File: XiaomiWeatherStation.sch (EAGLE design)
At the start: 12 parts, among them J1 1X2-3.5MM, K1 RELAY-SPDT, Q1 BD437

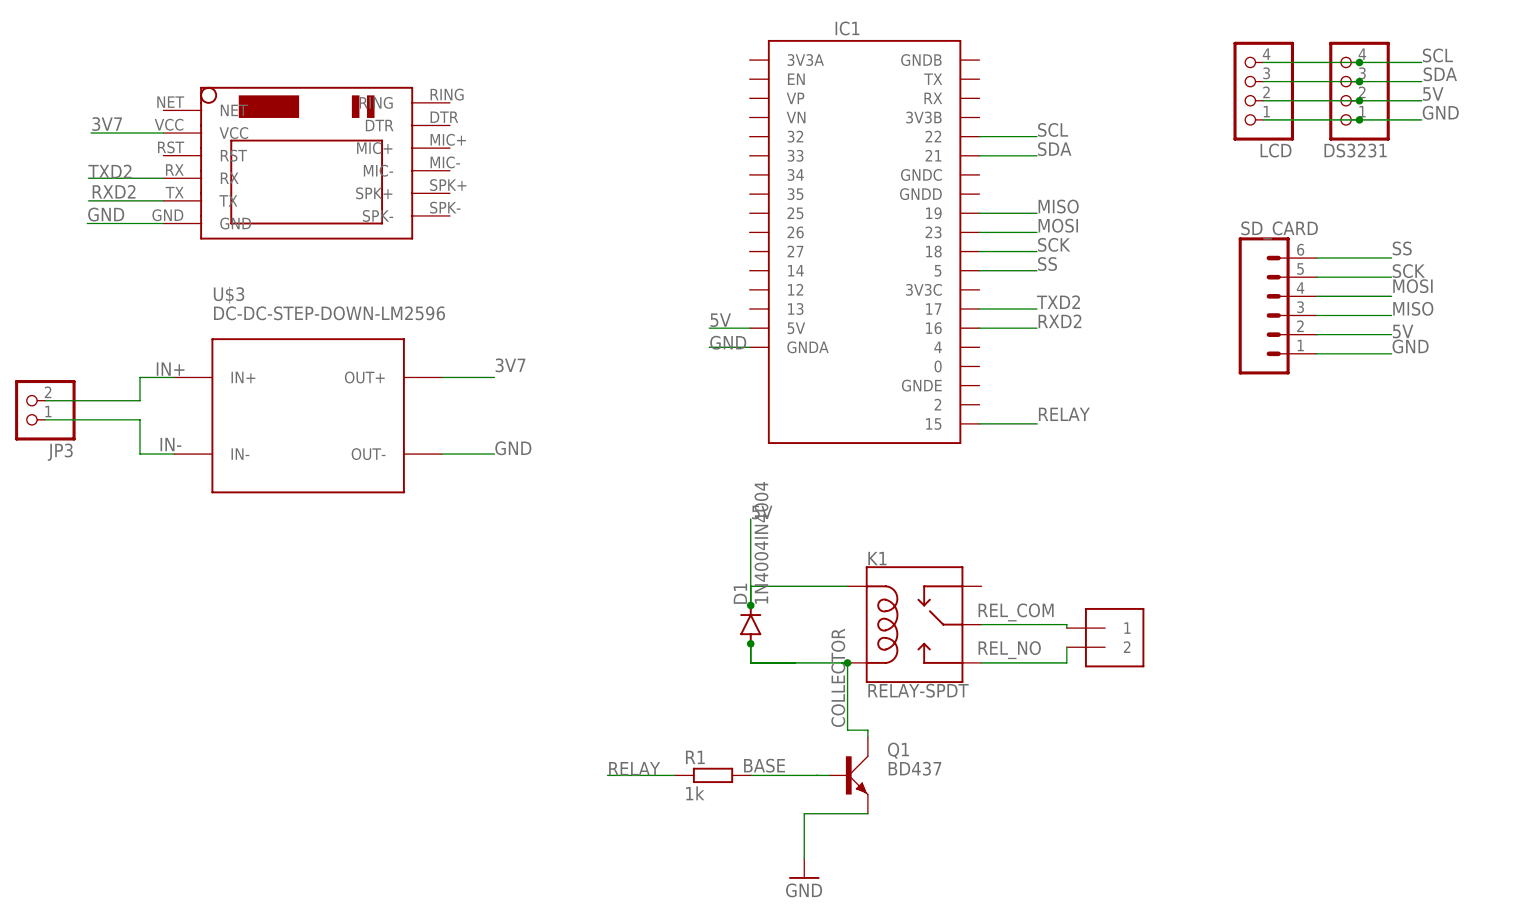
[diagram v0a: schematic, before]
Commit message: Adds actual sd and ds3231 components in place of header pins
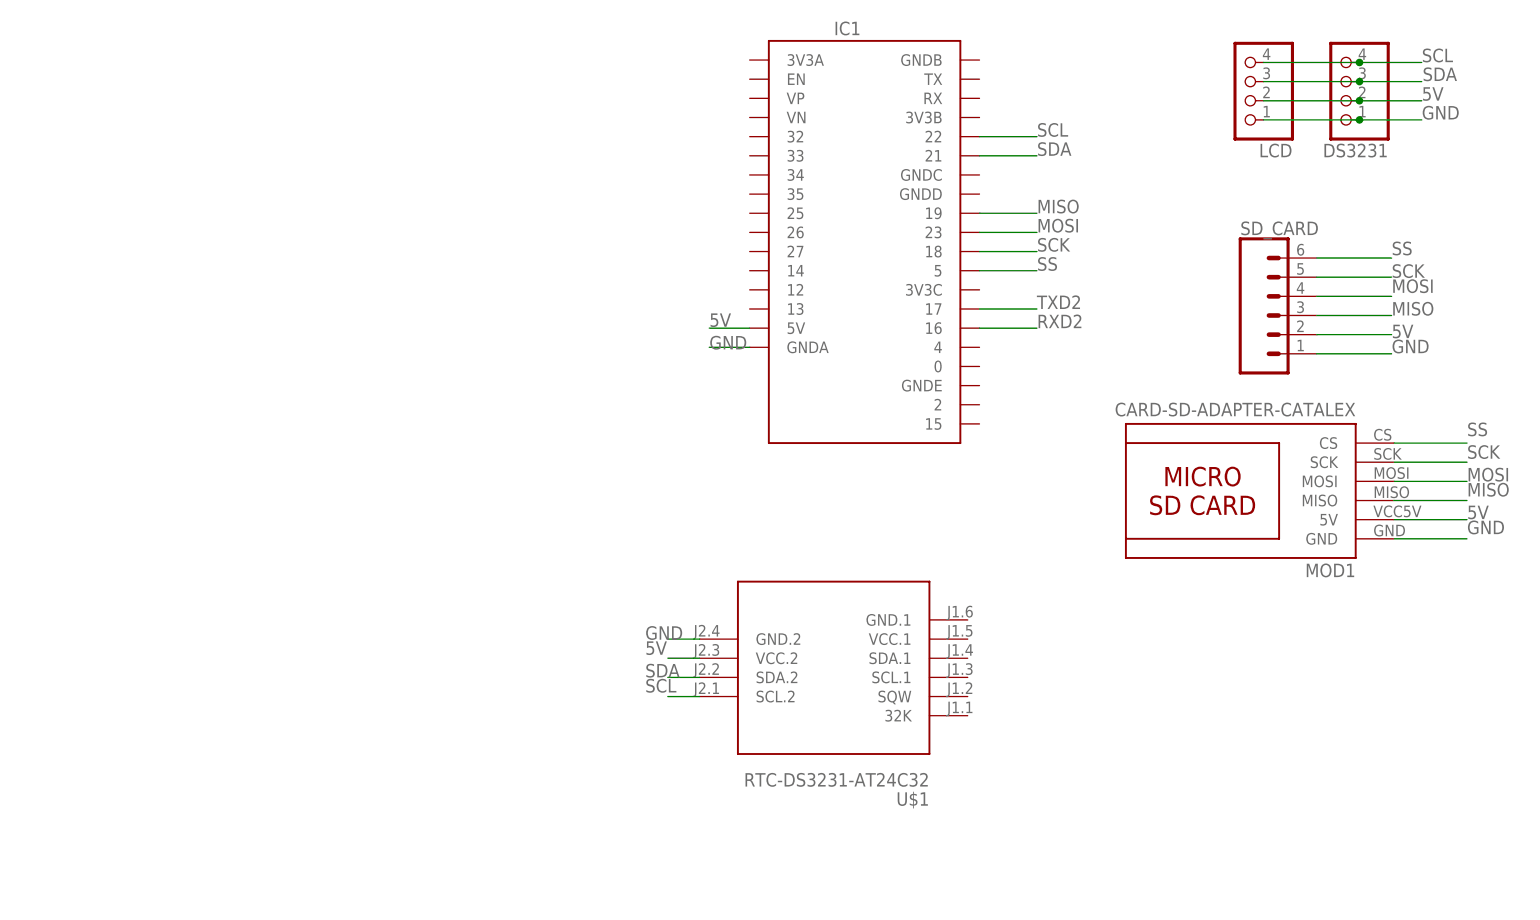
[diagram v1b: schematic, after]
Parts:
- removed D1: 1N4004IN4004, diode:1N4004IN4004
- removed J1: 1X2-3.5MM, adafruit:1X2-3.5MM
- removed JP3: (no value), pinhead:PINHD-1X2
- removed K1: RELAY-SPDT, SparkFun-Electromechanical:RELAY-SPDT
- removed Q1: BD437, transistor-power:BD437
- removed R1: 1k, rcl:R-EU_0204/7
- removed U$3: DC-DC-STEP-DOWN-LM2596, diy-modules:DC-DC-STEP-DOWN-LM2596
- added MOD1: CARD-SD-ADAPTER-CATALEX, SD-Card-Module_CATALEX:CARD-SD-ADAPTER-CATALEX
- U$1: value SIM800LMODULE -> RTC-DS3231-AT24C32; device SIM800LMODULE:SIM800LMODULE -> diy-modules:RTC-DS3231-AT24C32
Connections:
- removed net 3V7: U$1.VCC, U$3.OUT+
- removed net BASE: Q1.B, R1.2
- removed net COLLECTOR: D1.A, K1.COIL2, Q1.C
- removed net IN+: JP3.2, U$3.IN+
- removed net IN-: JP3.1, U$3.IN-
- removed net RELAY: IC1.15, R1.1
- removed net REL_COM: J1.1, K1.MAIN
- removed net REL_NO: J1.2, K1.NO
- net 5V: now also MOD1.5V, U$1.VCC.2; no longer D1.C, K1.COIL1
- net GND: now also MOD1.GND, U$1.GND.2; no longer Q1.E, U$1.GND, U$3.OUT-
- net MISO: now also MOD1.MISO
- net MOSI: now also MOD1.MOSI
- net RXD2: no longer U$1.TX
- net SCK: now also MOD1.SCK
- net SCL: now also U$1.SCL.2
- net SDA: now also U$1.SDA.2
- net SS: now also MOD1.CS
- net TXD2: no longer U$1.RX

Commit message: Completes design
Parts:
- removed DS3231: (no value), pinhead:PINHD-1X4
- removed SD_CARD: (no value), SparkFun-Connectors:CONN_06LONGPADS
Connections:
- net 5V: no longer DS3231.2, SD_CARD.2
- net GND: no longer DS3231.1, SD_CARD.1
- net MISO: no longer SD_CARD.3
- net MOSI: no longer SD_CARD.4
- net SCK: no longer SD_CARD.5
- net SCL: no longer DS3231.4
- net SDA: no longer DS3231.3
- net SS: no longer SD_CARD.6
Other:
- moved on the sheet: MOD1, U$1
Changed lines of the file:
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@@
 <part name="IC1" library="SSFD - ESP32 WEMOS LOLIN CHINA W_BATT" library_urn="urn:adsk.eagle:library:31562966" deviceset="SSFD_LOLIN32_WEMOS_CHINA_W_BATT" device="" package3d_urn="urn:adsk.eagle:package:31562973/2"/>
 <part name="LCD" library="pinhead" library_urn="urn:adsk.eagle:library:325" deviceset="PINHD-1X4" device="" package3d_urn="urn:adsk.eagle:package:22407/2"/>
-<part name="DS3231" library="pinhead" library_urn="urn:adsk.eagle:library:325" deviceset="PINHD-1X4" device="" package3d_urn="urn:adsk.eagle:package:22407/2"/>
 <part name="FRAME1" library="frames" library_urn="urn:adsk.eagle:library:229" deviceset="A3L-LOC" device=""/>
-<part name="SD_CARD" library="SparkFun-Connectors" library_urn="urn:adsk.eagle:library:31567038" deviceset="CONN_06" device="LONGPADS" package3d_urn="urn:adsk.eagle:package:31567581/1"/>
-<part name="MOD1" library="SD-Card-Module_CATALEX" library_urn="urn:adsk.eagle:library:31562955" deviceset="CARD-SD-ADAPTER-CATALEX" device="" package3d_urn="urn:adsk.eagle:package:31562959/1"/>
-<part name="U$1" library="diy-modules" library_urn="urn:adsk.eagle:library:31562516" deviceset="RTC-DS3231-AT24C32" device="" package3d_urn="urn:adsk.eagle:package:31562815/1"/>
+<part name="MOD1" library="SD-Card-Module_CATALEX" library_urn="urn:adsk.eagle:library:31562955" deviceset="CARD-SD-ADAPTER-CATALEX" device="" package3d_urn="urn:adsk.eagle:package:31562959/2"/>
+<part name="U$1" library="diy-modules" library_urn="urn:adsk.eagle:library:31562516" deviceset="RTC-DS3231-AT24C32" device="" package3d_urn="urn:adsk.eagle:package:31562815/3"/>
 </parts>
 <sheets>
@@
 <attribute name="VALUE" x="248.85" y="157.64" size="1.778" layer="96" rot="R180"/>
 </instance>
-<instance part="DS3231" gate="A" x="255.2" y="150.02" smashed="yes" rot="R180">
-<attribute name="NAME" x="261.55" y="141.765" size="1.778" layer="95" rot="R180"/>
-<attribute name="VALUE" x="261.55" y="157.64" size="1.778" layer="96" rot="R180"/>
-</instance>
 <instance part="FRAME1" gate="G$1" x="0" y="0" smashed="yes">
 <attribute name="DRAWING_NAME" x="344.17" y="15.24" size="2.54" layer="94"/>
@@
 <attribute name="SHEET" x="357.505" y="5.08" size="2.54" layer="94"/>
 </instance>
-<instance part="SD_CARD" gate="G$1" x="247" y="119" smashed="yes">
-<attribute name="VALUE" x="241.92" y="109.094" size="1.778" layer="96" font="vector"/>
-<attribute name="NAME" x="241.92" y="129.668" size="1.778" layer="95" font="vector"/>
+<instance part="MOD1" gate="MODULE" x="131" y="134" smashed="yes" rot="R180">
+<attribute name="NAME" x="146.24" y="123.078" size="1.778" layer="95" rot="R180"/>
+<attribute name="VALUE" x="146.24" y="142.636" size="1.778" layer="96" rot="MR0"/>
 </instance>
-<instance part="MOD1" gate="MODULE" x="242" y="97" smashed="yes" rot="R180">
-<attribute name="NAME" x="257.24" y="86.078" size="1.778" layer="95" rot="R180"/>
-<attribute name="VALUE" x="257.24" y="105.636" size="1.778" layer="96" rot="MR0"/>
-</instance>
-<instance part="U$1" gate="G$1" x="188" y="71" smashed="yes" rot="R180">
-<attribute name="NAME" x="200.7" y="55.76" size="1.778" layer="95" rot="R180"/>
-<attribute name="VALUE" x="200.7" y="58.3" size="1.778" layer="96" rot="R180"/>
+<instance part="U$1" gate="G$1" x="252" y="120" smashed="yes" rot="MR180">
+<attribute name="NAME" x="239.3" y="104.76" size="1.778" layer="95" rot="MR180"/>
+<attribute name="VALUE" x="239.3" y="107.3" size="1.778" layer="96" rot="MR180"/>
 </instance>
 </instances>
@@
 <segment>
 <pinref part="LCD" gate="A" pin="4"/>
-<pinref part="DS3231" gate="A" pin="4"/>
-<wire x1="245.04" y1="152.56" x2="257.74" y2="152.56" width="0.1524" layer="91"/>
-<wire x1="257.74" y1="152.56" x2="266" y2="152.56" width="0.1524" layer="91"/>
-<junction x="257.74" y="152.56"/>
+<wire x1="245.04" y1="152.56" x2="266" y2="152.56" width="0.1524" layer="91"/>
 <label x="266" y="152.6" size="1.778" layer="95"/>
 </segment>
 <segment>
 <pinref part="U$1" gate="G$1" pin="SCL.2"/>
-<wire x1="170.22" y1="68.46" x2="166" y2="68.46" width="0.1524" layer="91"/>
-<label x="163" y="69" size="1.778" layer="95"/>
+<wire x1="269.78" y1="117.46" x2="274" y2="117.46" width="0.1524" layer="91"/>
+<label x="277" y="118" size="1.778" layer="95" rot="MR0"/>
 </segment>
 </net>
@@
 <segment>
 <pinref part="LCD" gate="A" pin="3"/>
-<pinref part="DS3231" gate="A" pin="3"/>
-<wire x1="245.04" y1="150.02" x2="257.74" y2="150.02" width="0.1524" layer="91"/>
-<wire x1="257.74" y1="150.02" x2="266" y2="150.02" width="0.1524" layer="91"/>
-<junction x="257.74" y="150.02"/>
+<wire x1="245.04" y1="150.02" x2="266" y2="150.02" width="0.1524" layer="91"/>
 <label x="266.1" y="150.1" size="1.778" layer="95"/>
 </segment>
 <segment>
 <pinref part="U$1" gate="G$1" pin="SDA.2"/>
-<wire x1="170.22" y1="71" x2="166" y2="71" width="0.1524" layer="91"/>
-<label x="163" y="71" size="1.778" layer="95"/>
+<wire x1="269.78" y1="120" x2="274" y2="120" width="0.1524" layer="91"/>
+<label x="277" y="120" size="1.778" layer="95" rot="MR0"/>
 </segment>
 </net>
@@
 </segment>
 <segment>
-<pinref part="SD_CARD" gate="G$1" pin="3"/>
-<wire x1="252.08" y1="119" x2="262" y2="119" width="0.1524" layer="91"/>
-<label x="262" y="119" size="1.778" layer="95"/>
-</segment>
-<segment>
 <pinref part="MOD1" gate="MODULE" pin="MISO"/>
-<wire x1="262.32" y1="94.46" x2="272" y2="94.46" width="0.1524" layer="91"/>
-<label x="272" y="95" size="1.778" layer="95"/>
+<wire x1="151.32" y1="131.46" x2="161" y2="131.46" width="0.1524" layer="91"/>
+<label x="161" y="132" size="1.778" layer="95"/>
 </segment>
 </net>
@@
 </segment>
 <segment>
-<pinref part="SD_CARD" gate="G$1" pin="4"/>
-<wire x1="252.08" y1="121.54" x2="262" y2="121.54" width="0.1524" layer="91"/>
-<label x="262" y="122" size="1.778" layer="95"/>
-</segment>
-<segment>
 <pinref part="MOD1" gate="MODULE" pin="MOSI"/>
-<wire x1="262.32" y1="97" x2="272" y2="97" width="0.1524" layer="91"/>
-<label x="272" y="97" size="1.778" layer="95"/>
+<wire x1="151.32" y1="134" x2="161" y2="134" width="0.1524" layer="91"/>
+<label x="161" y="134" size="1.778" layer="95"/>
 </segment>
 </net>
@@
 </segment>
 <segment>
-<pinref part="SD_CARD" gate="G$1" pin="5"/>
-<wire x1="252.08" y1="124.08" x2="262" y2="124.08" width="0.1524" layer="91"/>
-<label x="262" y="124" size="1.778" layer="95"/>
-</segment>
-<segment>
 <pinref part="MOD1" gate="MODULE" pin="SCK"/>
-<wire x1="262.32" y1="99.54" x2="272" y2="99.54" width="0.1524" layer="91"/>
-<label x="272" y="100" size="1.778" layer="95"/>
+<wire x1="151.32" y1="136.54" x2="161" y2="136.54" width="0.1524" layer="91"/>
+<label x="161" y="137" size="1.778" layer="95"/>
 </segment>
 </net>
@@
 </segment>
 <segment>
-<pinref part="SD_CARD" gate="G$1" pin="6"/>
-<wire x1="252.08" y1="126.62" x2="262" y2="126.62" width="0.1524" layer="91"/>
-<label x="262" y="127" size="1.778" layer="95"/>
-</segment>
-<segment>
 <pinref part="MOD1" gate="MODULE" pin="CS"/>
-<wire x1="262.32" y1="102.08" x2="272" y2="102.08" width="0.1524" layer="91"/>
-<label x="272" y="103" size="1.778" layer="95"/>
+<wire x1="151.32" y1="139.08" x2="161" y2="139.08" width="0.1524" layer="91"/>
+<label x="161" y="140" size="1.778" layer="95"/>
 </segment>
 </net>
@@
 <segment>
 <pinref part="LCD" gate="A" pin="1"/>
-<pinref part="DS3231" gate="A" pin="1"/>
-<wire x1="245.04" y1="144.94" x2="257.74" y2="144.94" width="0.1524" layer="91"/>
-<wire x1="257.74" y1="144.94" x2="266" y2="144.94" width="0.1524" layer="91"/>
-<junction x="257.74" y="144.94"/>
+<wire x1="245.04" y1="144.94" x2="266" y2="144.94" width="0.1524" layer="91"/>
 <label x="266" y="145" size="1.778" layer="95"/>
 </segment>
 <segment>
-<pinref part="SD_CARD" gate="G$1" pin="1"/>
-<wire x1="252.08" y1="113.92" x2="262" y2="113.92" width="0.1524" layer="91"/>
-<label x="262" y="114" size="1.778" layer="95"/>
-</segment>
-<segment>
 <pinref part="U$1" gate="G$1" pin="GND.2"/>
-<wire x1="170.22" y1="76.08" x2="166" y2="76.08" width="0.1524" layer="91"/>
-<label x="163" y="76" size="1.778" layer="95"/>
+<wire x1="269.78" y1="125.08" x2="274" y2="125.08" width="0.1524" layer="91"/>
+<label x="277" y="125" size="1.778" layer="95" rot="MR0"/>
 </segment>
 <segment>
 <pinref part="MOD1" gate="MODULE" pin="GND"/>
-<wire x1="262.32" y1="89.38" x2="272" y2="89.38" width="0.1524" layer="91"/>
-<label x="272" y="90" size="1.778" layer="95"/>
+<wire x1="151.32" y1="126.38" x2="161" y2="126.38" width="0.1524" layer="91"/>
+<label x="161" y="127" size="1.778" layer="95"/>
 </segment>
 </net>
@@
 <segment>
 <pinref part="LCD" gate="A" pin="2"/>
-<pinref part="DS3231" gate="A" pin="2"/>
-<wire x1="245.04" y1="147.48" x2="257.74" y2="147.48" width="0.1524" layer="91"/>
-<wire x1="257.74" y1="147.48" x2="266" y2="147.48" width="0.1524" layer="91"/>
-<junction x="257.74" y="147.48"/>
+<wire x1="245.04" y1="147.48" x2="266" y2="147.48" width="0.1524" layer="91"/>
 <label x="266" y="147.5" size="1.778" layer="95"/>
 </segment>
 <segment>
-<pinref part="SD_CARD" gate="G$1" pin="2"/>
-<wire x1="252.08" y1="116.46" x2="262" y2="116.46" width="0.1524" layer="91"/>
-<label x="262" y="116" size="1.778" layer="95"/>
-</segment>
-<segment>
 <pinref part="U$1" gate="G$1" pin="VCC.2"/>
-<wire x1="170.22" y1="73.54" x2="166" y2="73.54" width="0.1524" layer="91"/>
-<label x="163" y="74" size="1.778" layer="95"/>
+<wire x1="269.78" y1="122.54" x2="274" y2="122.54" width="0.1524" layer="91"/>
+<label x="277" y="123" size="1.778" layer="95" rot="MR0"/>
 </segment>
 <segment>
 <pinref part="MOD1" gate="MODULE" pin="5V"/>
-<wire x1="262.32" y1="91.92" x2="272" y2="91.92" width="0.1524" layer="91"/>
-<label x="272" y="92" size="1.778" layer="95"/>
+<wire x1="151.32" y1="128.92" x2="161" y2="128.92" width="0.1524" layer="91"/>
+<label x="161" y="129" size="1.778" layer="95"/>
 </segment>
 </net>
